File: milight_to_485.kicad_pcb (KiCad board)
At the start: 2 copper layers, 50 x 50 mm, 25 parts, among them J1 RJ12, J2 RJ45, P1 SWIM, P2 CONN_01X02, SW1 reset, U1 LT8900, U2 STM8S103F3, U3 MAX487, U4 74HC245, U5 MC78M05CDT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

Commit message: PCB upd
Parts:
- moved R1 11.8 mm to (114.4, 82.2)
- moved C6 10.4 mm to (116.5, 82.2)
- moved SW1 10.3 mm to (119.8, 78.2)
- moved C1 2.16 mm to (127.7, 82.7)
- moved C2 2.10 mm to (127.7, 84.8)
- moved P2 0.65 mm to (102.1, 90.0)
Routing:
- net GND: track 0.00 -> 60.8 mm, vias 0 -> 3
- net +5V: track 0.00 -> 37.7 mm
- net /MISO: track 0.00 -> 31.2 mm
- net /MOSI: track 0.00 -> 28.3 mm
- net /SCK: track 0.00 -> 25.4 mm
- net /DE: track 0.00 -> 23.1 mm, vias 0 -> 2
- net /NRST: track 0.00 -> 19.0 mm
- net /TxD: track 0.00 -> 18.6 mm
- net /VIN: track 0.00 -> 15.1 mm
- net +3V3: track 0.00 -> 14.7 mm
- net /485_A: track 0.00 -> 9.05 mm
- net /PWM4: track 0.00 -> 6.72 mm
- net /PWM2: track 0.00 -> 6.20 mm
- net /485_B: track 0.00 -> 6.05 mm
- net Net-(C2-Pad1): track 0.00 -> 4.51 mm
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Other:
- net class Default: clearance 0.2 -> 0.25
- rule trace_clearance: 0.2 -> 0.25

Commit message: PCB update
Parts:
- added ?: Symbol_OSHW-Logo_SilkScreen, Symbols:Symbol_OSHW-Logo_SilkScreen, F.Cu at (144.6, 77.5)
- added ?: Symbol_OSHW-Logo_CopperTop_Negative, Symbols:Symbol_OSHW-Logo_CopperTop_Negative, B.Cu at (121.5, 53.5)
- moved C4 5.78 mm to (127.2, 66.4), turned to 0 degrees
- moved C3 5.74 mm to (127.2, 68.5), turned to 0 degrees
- renumbered SW1 to RST
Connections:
- J1 pad 1: (no net) -> Net-(J1-Pad1)
- J1 pad 5: (no net) -> Net-(J1-Pad5)
- J1 pad 6: (no net) -> Net-(J1-Pad6)
- J1 pad 7: (no net) -> Net-(J1-Pad7)
- J1 pad 8: (no net) -> Net-(J1-Pad8)
- J2 pad 1: (no net) -> Net-(J2-Pad1)
- J2 pad 8: (no net) -> +5V
- U1 pad 8: (no net) -> Net-(U1-Pad8)
- U2 pad 11: (no net) -> Net-(U2-Pad11)
- U2 pad 12: (no net) -> Net-(U2-Pad12)
- U4 pad 11: (no net) -> Net-(U4-Pad11)
- U4 pad 12: (no net) -> Net-(U4-Pad12)
- U4 pad 13: (no net) -> Net-(U4-Pad13)
- U4 pad 7: (no net) -> Net-(U4-Pad7)
- U4 pad 8: (no net) -> Net-(U4-Pad8)
- U4 pad 9: (no net) -> Net-(U4-Pad9)
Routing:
- net +3V3: track 14.7 -> 85.5 mm, vias 0 -> 5
- net +5V: track 37.7 -> 82.0 mm, vias 0 -> 4
- net /PWM2_3: track 0.00 -> 29.1 mm, vias 0 -> 2
- net /CSN: track 0.00 -> 26.3 mm, vias 0 -> 1
- net /PWM2_1: track 0.00 -> 24.4 mm, vias 0 -> 2
- net /PKT: track 0.00 -> 24.1 mm, vias 0 -> 1
- net /SWIM: track 0.00 -> 23.7 mm
- net /PWM1_3: track 0.00 -> 18.8 mm, vias 0 -> 2
- net /PWM2_2: track 0.00 -> 18.7 mm
- net /PWM1_4: track 0.00 -> 17.6 mm
- net /RxD: track 1.64 -> 16.0 mm
- net /NRST: track 19.0 -> 31.9 mm
- net GND: track 60.8 -> 67.9 mm, vias 3 -> 6
- net /MISO: track 31.2 -> 26.6 mm
- net /MOSI: track 28.3 -> 24.0 mm
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- added copper zone on B.Cu, net GND
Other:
- net class Default: clearance 0.25 -> 0.2
- rule trace_clearance: 0.25 -> 0.2
- board text added: "485-RF-PWM V1"
- board text added: "BK 2016"
- board text added: "RF-485-PWM V1"

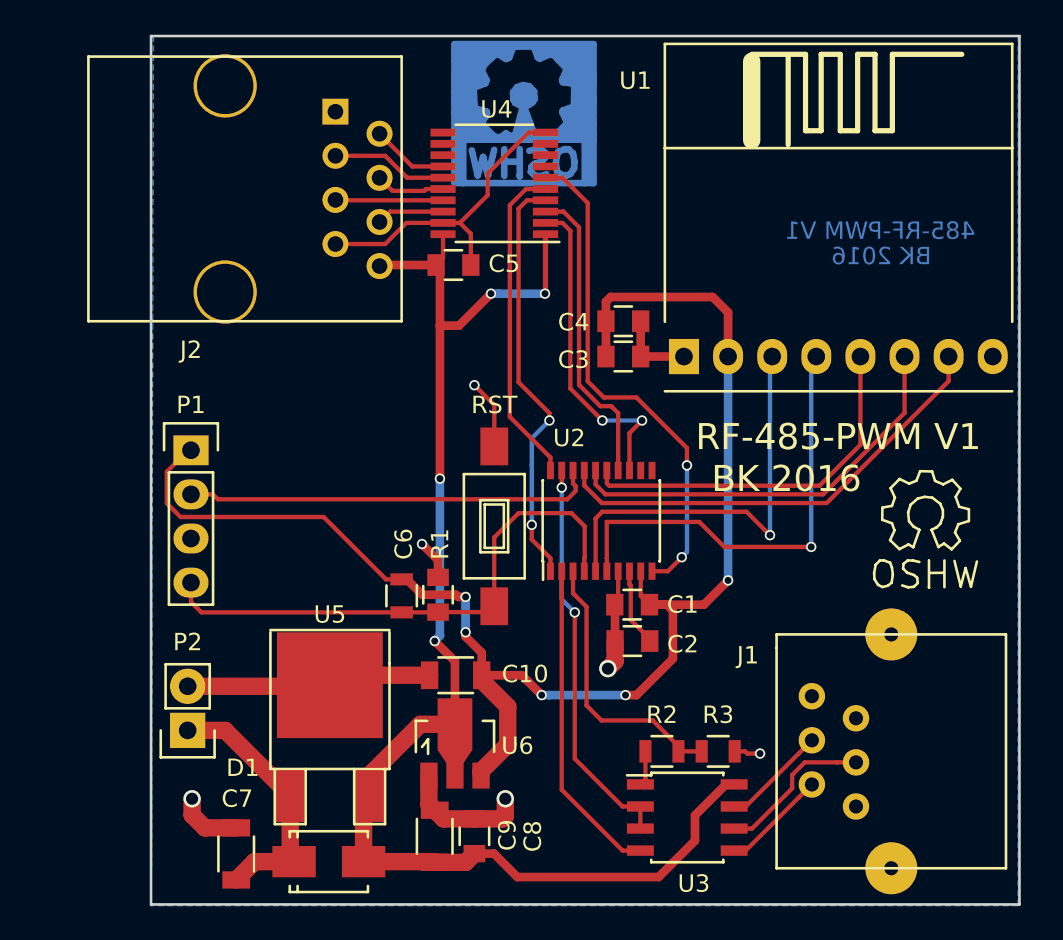
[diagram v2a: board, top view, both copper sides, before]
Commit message: PCB Update TTL Output Added
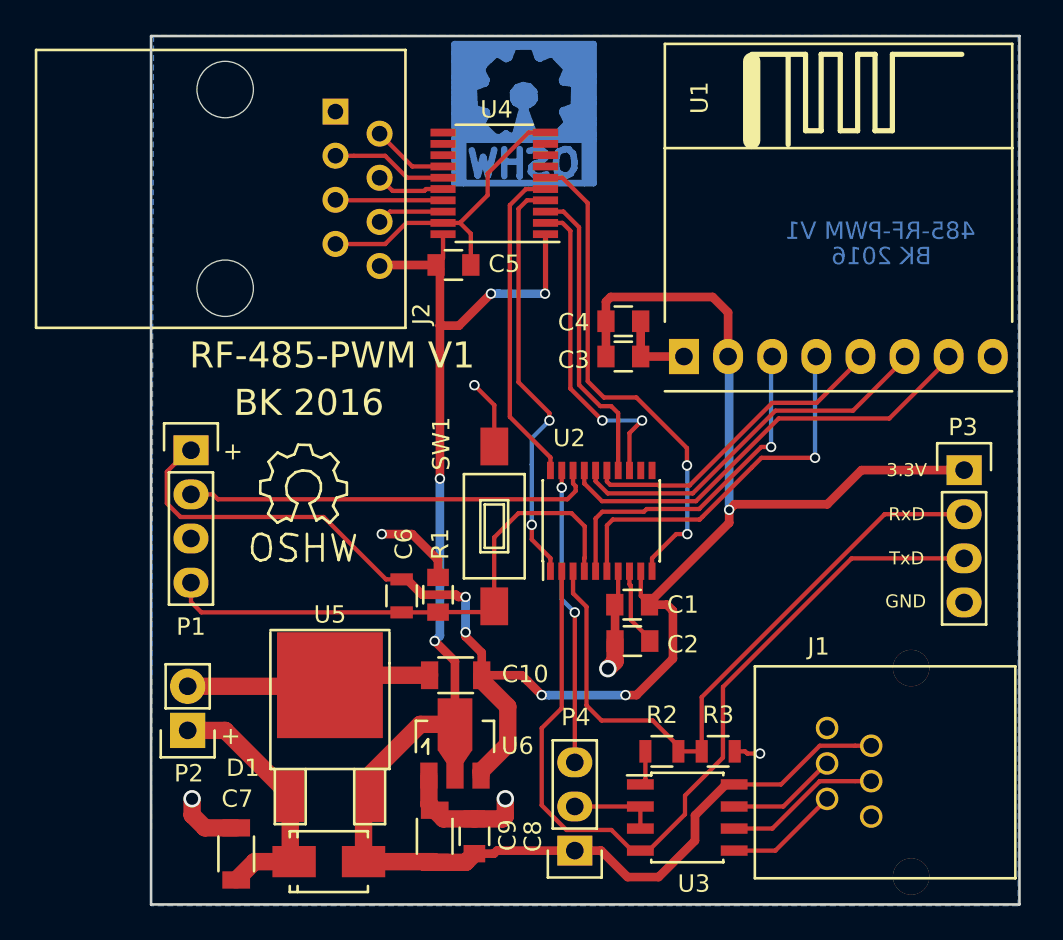
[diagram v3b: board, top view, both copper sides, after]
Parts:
- added P3: TTL, Pin_Headers:Pin_Header_Straight_1x04, F.Cu at (146.8, 75.0)
- added P4: TTL_SW, Pin_Headers:Pin_Header_Straight_1x03, F.Cu at (124.4, 96.9)
- J1: footprint Connect:RJ12_E -> BK_Common:RJ12_2mm_Pitch
- J2: footprint Connect:RJ45_8 -> BK_Common:RJ45_UnShielded
- U1: footprint LT8900_2.54mmPitch_20x20 -> BK_Common:LT8900_2.54mmPitch_20x20
- moved ? 35.8 mm to (108.8, 76.0)
- moved J1 3.44 mm to (143.8, 92.4)
- renumbered RST to SW1
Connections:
- J1 pad 1: Net-(J1-Pad1) -> (no net)
- J1 pad 5: Net-(J1-Pad5) -> +5V
- J1 pad 6: Net-(J1-Pad6) -> (no net)
- J1 pad 7: Net-(J1-Pad7) -> (no net)
- J1 pad 8: Net-(J1-Pad8) -> (no net)
- J2 pad 1: Net-(J2-Pad1) -> (no net)
- U1 pad 8: Net-(U1-Pad8) -> (no net)
- U2 pad 11: Net-(U2-Pad11) -> (no net)
- U2 pad 12: Net-(U2-Pad12) -> (no net)
- U3 pad 2: /DE -> /DE_O
- U3 pad 3: /DE -> /DE_O
- U4 pad 11: Net-(U4-Pad11) -> (no net)
- U4 pad 12: Net-(U4-Pad12) -> (no net)
- U4 pad 13: Net-(U4-Pad13) -> (no net)
- U4 pad 7: Net-(U4-Pad7) -> (no net)
- U4 pad 8: Net-(U4-Pad8) -> (no net)
- U4 pad 9: Net-(U4-Pad9) -> (no net)
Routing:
- net /TxD: track 18.6 -> 49.3 mm
- net /RxD: track 16.0 -> 38.5 mm
- net +3V3: track 85.5 -> 98.2 mm
- net +5V: track 82.0 -> 91.0 mm
- net /DE: track 23.1 -> 17.1 mm
- net /DE_O: track 0.00 -> 5.05 mm
- net /PKT: track 24.1 -> 20.3 mm
- net /CSN: track 26.3 -> 22.5 mm
- net GND: track 67.9 -> 71.6 mm
- net /SCK: track 21.5 -> 18.5 mm
- net /MOSI: track 24.0 -> 22.1 mm
- net /485_B: track 6.05 -> 7.04 mm
- net /MISO: track 26.6 -> 25.7 mm
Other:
- board text added: "+"
- board text added: "3.3V"
- board text added: "GND"
- board text added: "RxD"
- board text added: "TxD"
